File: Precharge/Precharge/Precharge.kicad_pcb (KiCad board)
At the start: 2 copper layers, 133 x 98 mm, 121 parts, among them J1 MicroFit, J2 Mini-Fit_Jr_5566-04A, J3 Micro-Fit 43045-0212, K1 OMRON-G2RL-24, K2 G7L-2A-X-L, Q1 2N7002, Q2 MMBT3906, Q3 2N7002, U1 TJA1051T-3, U10 LM393, U11 4N35, U2 SPAN02A-12, U3 Teensy4.0, U4 LM1117-5.0, U5 4N35, U6 4N35, U7 LM331, U8 LM331, U9 LM2904

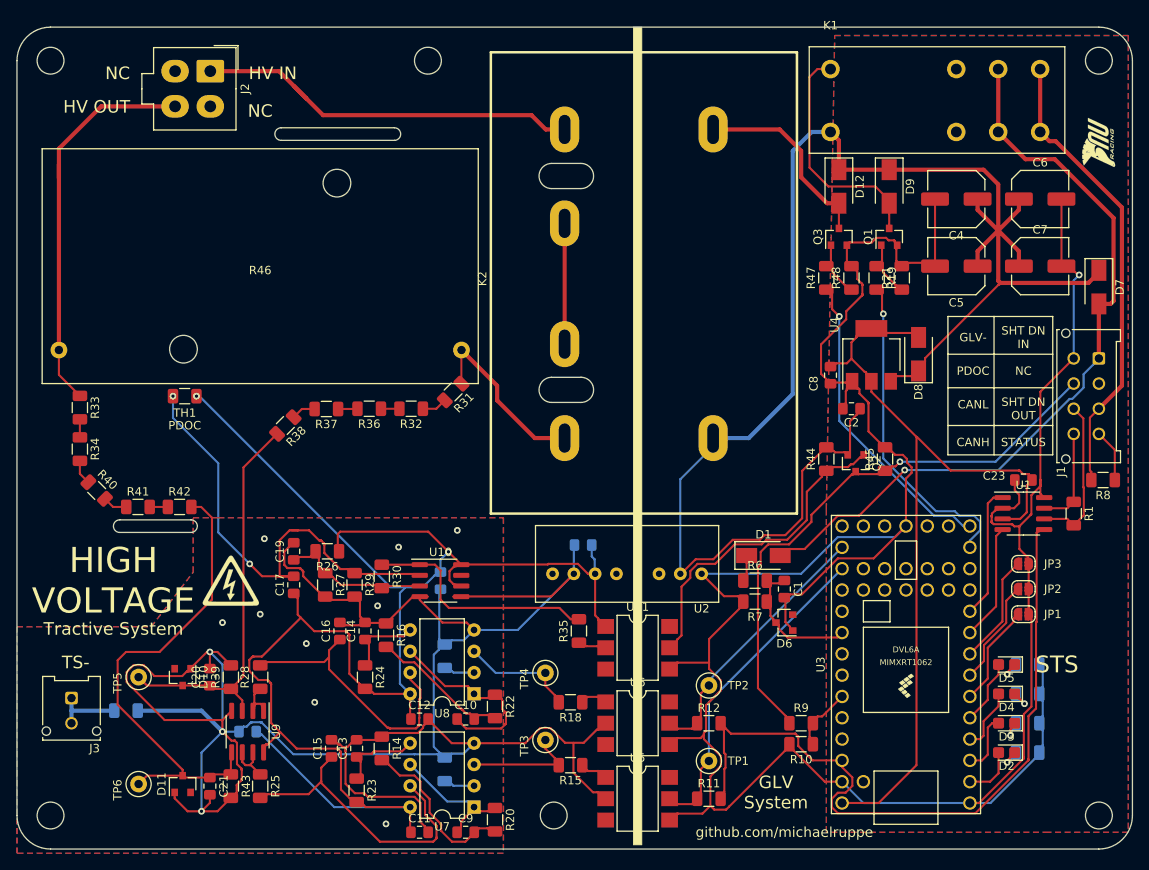
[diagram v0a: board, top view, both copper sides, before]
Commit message: :hammer: update board routing to reflect bodges made in prototyping
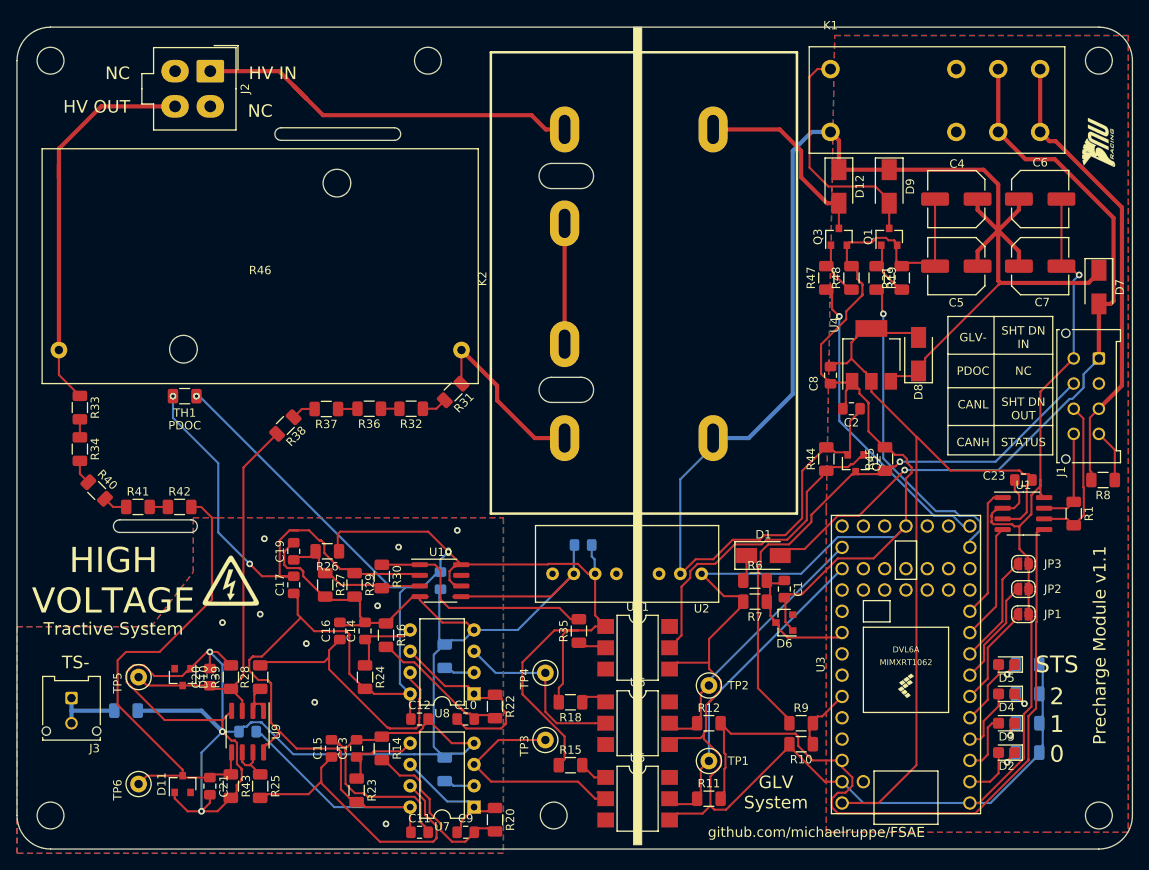
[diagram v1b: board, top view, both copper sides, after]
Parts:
- R10, R7: value 7k -> 6k8
- R23, R24: value 10k -> 6k8
- R31, R32, R33, R34, R36, R37, R38, R40, R41, R42: value 500k -> 510k
- R35: value 560 -> 2k2
- R39, R43: value 40k -> 39k
- turned R15 to 0 degrees
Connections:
- R15 pad 1: /FoutTS -> +12P
- R18 pad 1: /FoutAccu -> Net-(R18-Pad1)
- R18 pad 2: Net-(R18-Pad2) -> +12P
- TP3 pad 1: Net-(R15-Pad2) -> /FoutTS
- TP4 pad 1: Net-(R18-Pad2) -> /FoutAccu
- U5 pad 1: /FoutTS -> Net-(R15-Pad2)
- U5 pad 2: GNDS -> /FoutTS
- U6 pad 1: /FoutAccu -> Net-(R18-Pad1)
- U6 pad 2: GNDS -> /FoutAccu
- U7 pad 3: Net-(R15-Pad2) -> /FoutTS
- U8 pad 3: Net-(R18-Pad2) -> /FoutAccu
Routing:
- net +12P: track 200.1 -> 237.7 mm
- net GNDS: track 282.4 -> 255.7 mm
- net /FoutTS: track 3.37 -> 27.2 mm
- net /FoutAccu: track 3.25 -> 23.1 mm
- net Net-(R18-Pad2): track 13.7 -> 0.00 mm
- net Net-(R15-Pad2): track 13.7 -> 4.56 mm
- net Net-(R18-Pad1): track 0.00 -> 3.25 mm
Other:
- board text added: "0"
- board text added: "1"
- board text added: "2"
- board text added: "Precharge Module v1.1"
- board text added: "github.com/michaelruppe/FSAE"
- board text removed: "github.com/michaelruppe"
